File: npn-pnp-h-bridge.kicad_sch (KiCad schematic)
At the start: 41 parts, among them J1 S4B-PH-K-S_LF__SN_, J2 S2B-PH-K-S_LF__SN_, Q1 MMBT3904, Q2 MMBT3904, Q3 MMBT3904, Q4 MMBT3904

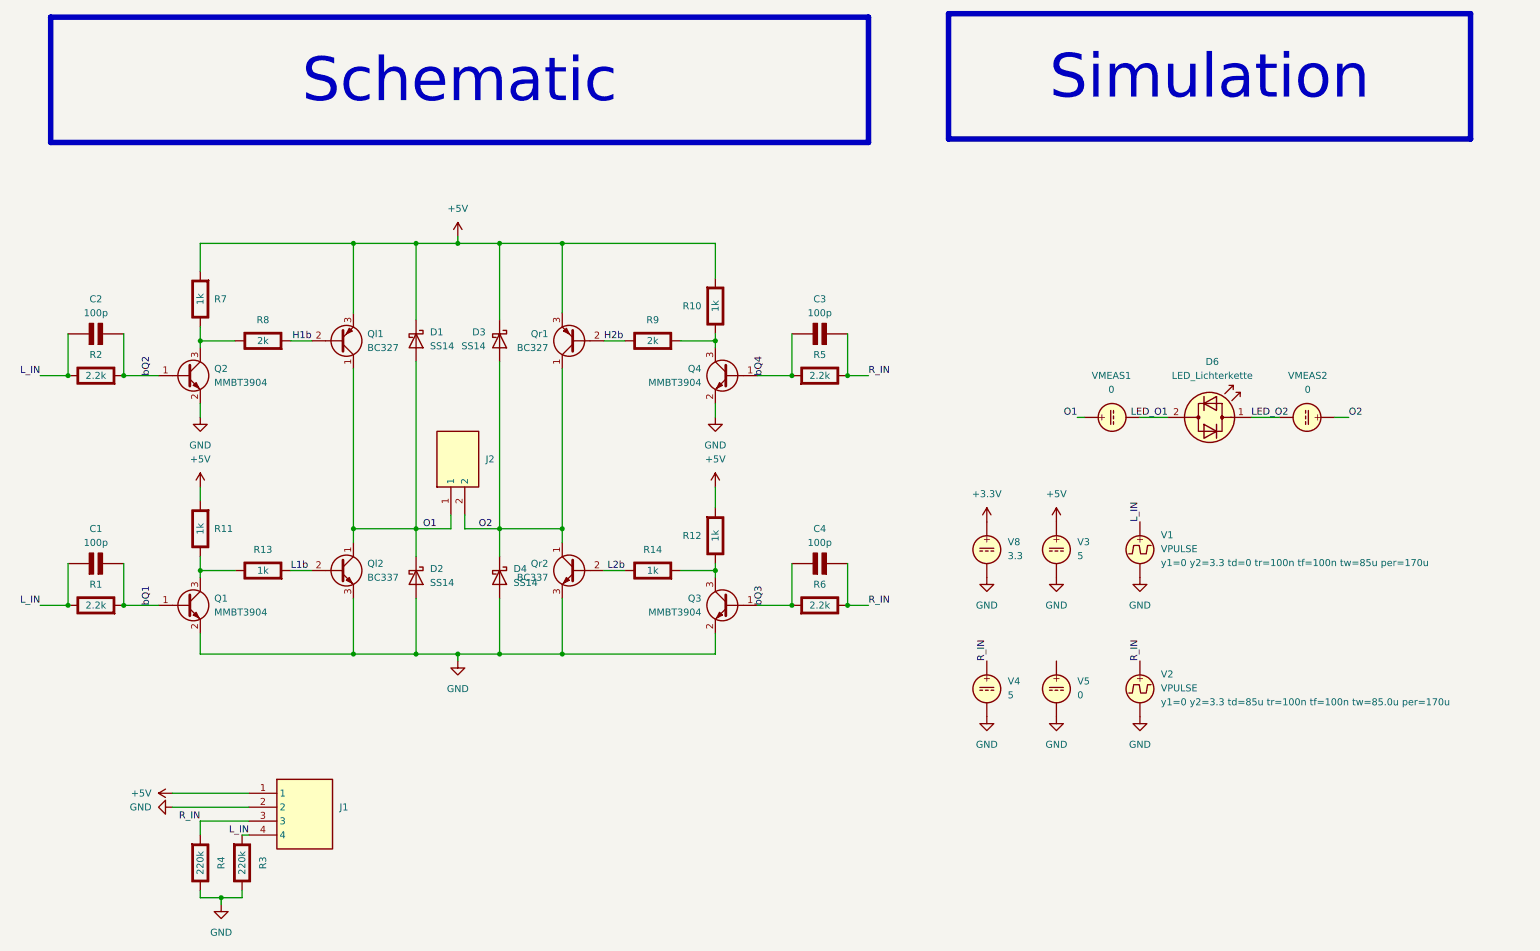
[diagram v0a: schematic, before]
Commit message: Update README with current measurements; optimize resistor values for up to 500mA load
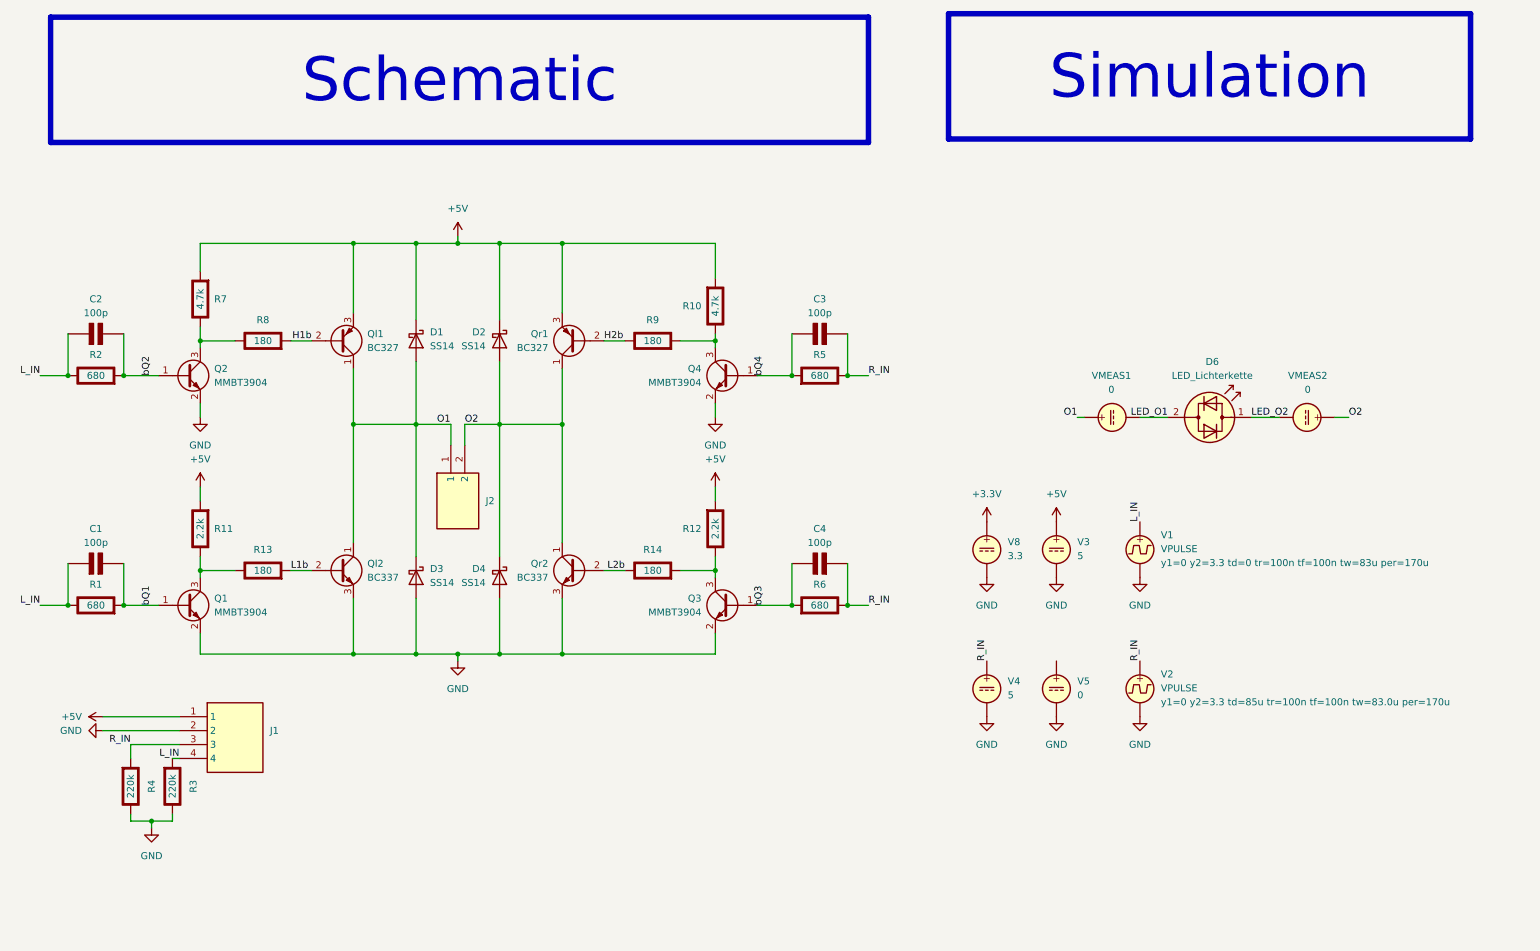
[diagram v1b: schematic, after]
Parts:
- R1, R2, R5, R6: value 2.2k -> 680
- R10, R7: value 1k -> 4.7k
- R11, R12: value 1k -> 2.2k
- R13, R14: value 1k -> 180
- R8, R9: value 2k -> 180
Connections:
- net +5V: now also D2.1 (K); no longer D3.1 (K)
- net GND: now also D3.2 (A); no longer D2.2 (A)
- net O1: now also D3.1 (K); no longer D2.1 (K)
- net O2: now also D2.2 (A); no longer D3.2 (A)
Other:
- moved on the sheet: J1, J2, R12, R3, R4

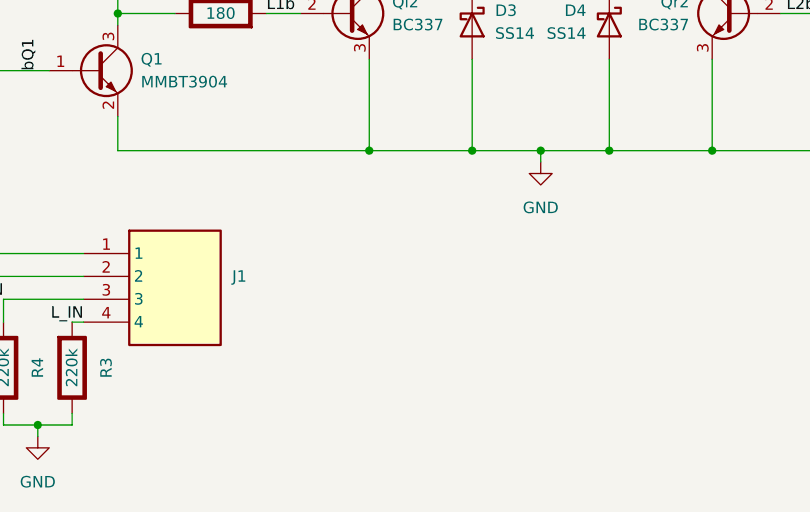
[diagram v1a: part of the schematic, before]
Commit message: Make PCB stackable via 2x03 connheader
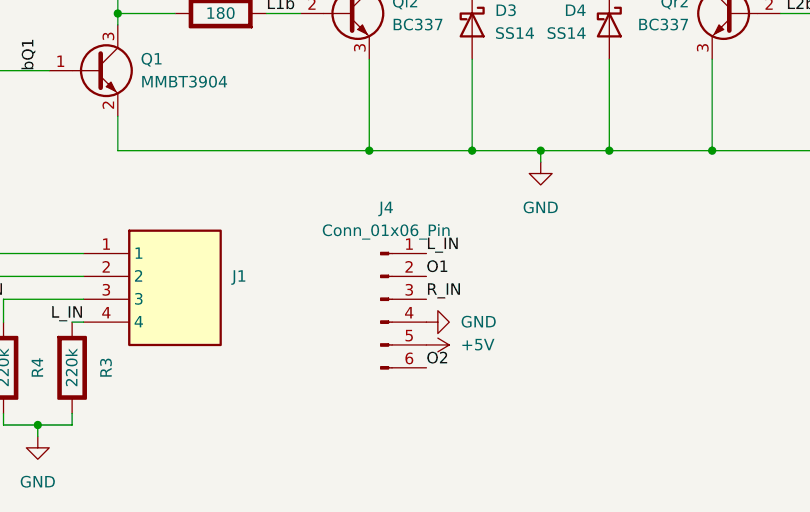
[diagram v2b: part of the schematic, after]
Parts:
- added J4: Conn_01x06_Pin, Connector_PinHeader_2.54mm:PinHeader_2x03_P2.54mm_Vertical, symbol Connector:Conn_01x06_Pin
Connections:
- net +5V: now also J4.5 (Pin_5)
- net GND: now also J4.4 (Pin_4)
- net L_IN: now also J4.1 (Pin_1)
- net O1: now also J4.2 (Pin_2)
- net O2: now also J4.6 (Pin_6)
- net R_IN: now also J4.3 (Pin_3)
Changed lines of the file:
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@@
 		)
 	)
+	(label "O1"
+		(at 81.28 154.94 0)
+		(effects
+			(font
+				(size 1.27 1.27)
+			)
+			(justify left bottom)
+		)
+	)
 	(label "H1b"
 		(at 67.31 83.82 180)
@@
 		)
 	)
+	(label "R_IN"
+		(at 81.28 157.48 0)
+		(effects
+			(font
+				(size 1.27 1.27)
+			)
+			(justify left bottom)
+		)
+	)
 	(label "O1"
 		(at 90.17 99.06 0)
@@
 	)
 	(label "L_IN"
+		(at 81.28 152.4 0)
+		(effects
+			(font
+				(size 1.27 1.27)
+			)
+			(justify left bottom)
+		)
+	)
+	(label "L_IN"
 		(at 218.44 116.84 90)
 		(effects
@@
 		)
 	)
+	(label "O2"
+		(at 81.28 165.1 0)
+		(effects
+			(font
+				(size 1.27 1.27)
+			)
+			(justify left bottom)
+		)
+	)
 	(label "bQ4"
 		(at 149.86 90.17 90)
@@
 	)
 	(symbol
+		(lib_id "Connector:Conn_01x06_Pin")
+		(at 76.2 157.48 0)
+		(unit 1)
+		(exclude_from_sim no)
+		(in_bom yes)
+		(on_board yes)
+		(dnp no)
+		(fields_autoplaced yes)
+		(property "Reference" "J4"
+			(at 76.835 147.32 0)
+			(effects
+				(font
+					(size 1.27 1.27)
+				)
+			)
+		)
+		(property "Value" "Conn_01x06_Pin"
+			(at 76.835 149.86 0)
+			(effects
+				(font
+					(size 1.27 1.27)
+				)
+			)
+		)
+		(property "Footprint" "Connector_PinHeader_2.54mm:PinHeader_2x03_P2.54mm_Vertical"
+			(at 76.2 157.48 0)
+			(effects
+				(font
+					(size 1.27 1.27)
+				)
+				(hide yes)
+			)
+		)
+		(property "Datasheet" "~"
+			(at 76.2 157.48 0)
+			(effects
+				(font
+					(size 1.27 1.27)
+				)
+				(hide yes)
+			)
+		)
+		(property "Description" "Generic connector, single row, 01x06, script generated"
+			(at 76.2 157.48 0)
+			(effects
+				(font
+					(size 1.27 1.27)
+				)
+				(hide yes)
+			)
+		)
+		(pin "5"
+		)
+		(pin "1"
+		)
+		(pin "6"
+		)
+		(pin "2"
+		)
+		(pin "3"
+		)
+		(pin "4"
+		)
+		(instances
+			(project "npn-pnp-h-bridge"
+				(path "/225c2104-9470-41e6-a40d-f9d3cc65f923"
+					(reference "J4")
+					(unit 1)
+				)
+			)
+		)
+	)
+	(symbol
 		(lib_id "Transistor_BJT:MMBT3904")
 		(at 44.45 90.17 0)
@@
 	(symbol
 		(lib_id "power:GND")
+		(at 81.28 160.02 90)
+		(unit 1)
+		(exclude_from_sim no)
+		(in_bom yes)
+		(on_board yes)
+		(dnp no)
+		(fields_autoplaced yes)
+		(property "Reference" "#PWR018"
+			(at 87.63 160.02 0)
+			(effects
+				(font
+					(size 1.27 1.27)
+				)
+				(hide yes)
+			)
+		)
+		(property "Value" "GND"
+			(at 85.09 160.0199 90)
+			(effects
+				(font
+					(size 1.27 1.27)
+				)
+				(justify right)
+			)
+		)
+		(property "Footprint" ""
+			(at 81.28 160.02 0)
+			(effects
+				(font
+					(size 1.27 1.27)
+				)
+				(hide yes)
+			)
+		)
+		(property "Datasheet" ""
+			(at 81.28 160.02 0)
+			(effects
+				(font
+					(size 1.27 1.27)
+				)
+				(hide yes)
+			)
+		)
+		(property "Description" "Power symbol creates a global label with name \"GND\" , ground"
+			(at 81.28 160.02 0)
+			(effects
+				(font
+					(size 1.27 1.27)
+				)
+				(hide yes)
+			)
+		)
+		(pin "1"
+		)
+		(instances
+			(project "npn-pnp-h-bridge"
+				(path "/225c2104-9470-41e6-a40d-f9d3cc65f923"
+					(reference "#PWR018")
+					(unit 1)
+				)
+			)
+		)
+	)
+	(symbol
+		(lib_id "power:GND")
 		(at 203.2 127 0)
 		(unit 1)
@@
 					(unit 1)
 				)
+			)
+		)
+	)
+	(symbol
+		(lib_id "power:+5V")
+		(at 81.28 162.56 270)
+		(unit 1)
+		(exclude_from_sim no)
+		(in_bom yes)
+		(on_board yes)
+		(dnp no)
+		(fields_autoplaced yes)
+		(property "Reference" "#PWR014"
+			(at 77.47 162.56 0)
+			(effects
+				(font
+					(size 1.27 1.27)
+				)
+				(hide yes)
+			)
+		)
+		(property "Value" "+5V"
+			(at 85.09 162.5599 90)
+			(effects
+				(font
+					(size 1.27 1.27)
+				)
+				(justify left)
+			)
+		)
+		(property "Footprint" ""
+			(at 81.28 162.56 0)
+			(effects
+				(font
+					(size 1.27 1.27)
+				)
+				(hide yes)
+			)
+		)
+		(property "Datasheet" ""
+			(at 81.28 162.56 0)
+			(effects
+				(font
+					(size 1.27 1.27)
+				)
+				(hide yes)
+			)
+		)
+		(property "Description" "Power symbol creates a global label with name \"+5V\""
+			(at 81.28 162.56 0)
+			(effects
+				(font
+					(size 1.27 1.27)
+				)
+				(hide yes)
+			)
+		)
+		(pin "1"
+		)
+		(instances
+			(project "npn-pnp-h-bridge"
+				(path "/225c2104-9470-41e6-a40d-f9d3cc65f923"
+					(reference "#PWR014")
+					(unit 1)
+				)

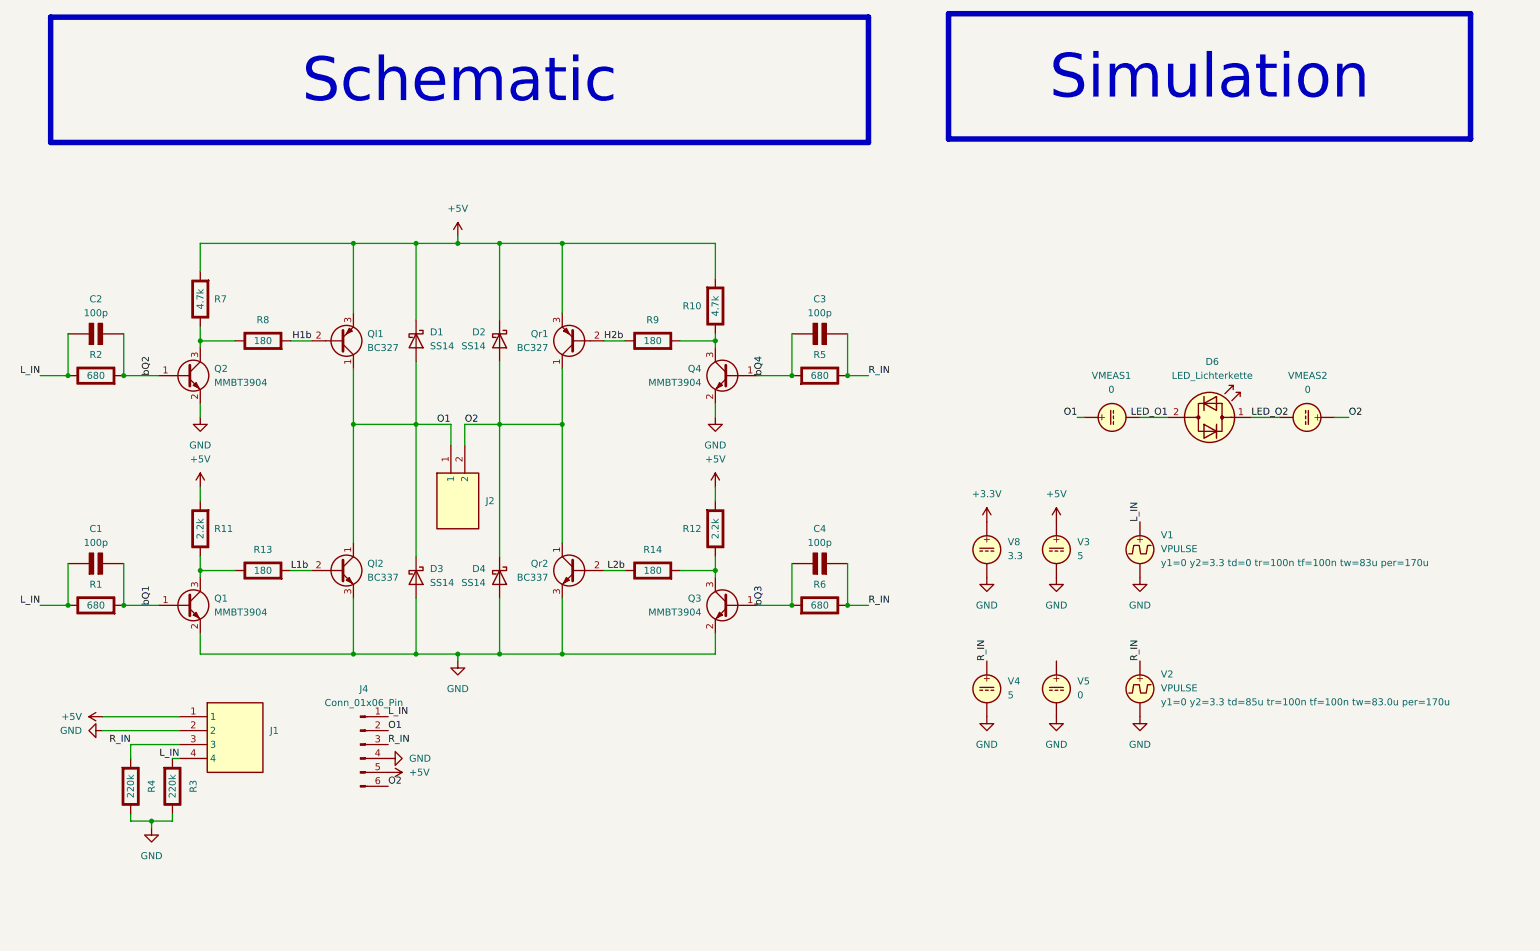
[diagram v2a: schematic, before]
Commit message: add caps to gnd for the h-bridge bases
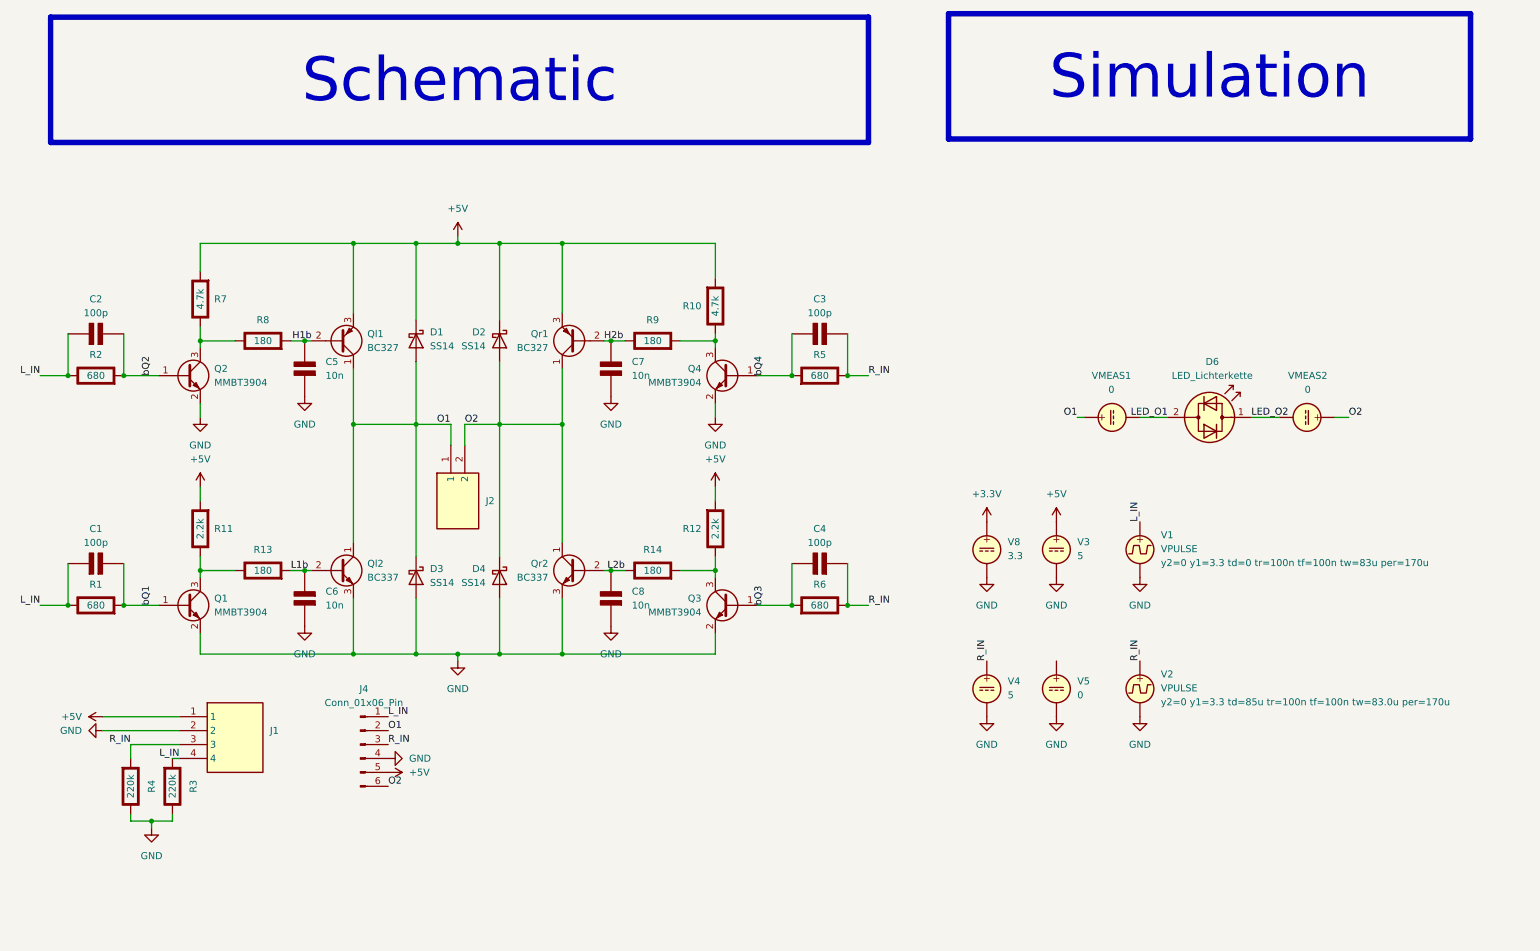
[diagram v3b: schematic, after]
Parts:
- added C5, C6, C7, C8: 10n, Capacitor_SMD:C_0805_2012Metric_Pad1.18x1.45mm_HandSolder, symbol PCM_Elektuur:C
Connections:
- net GND: now also C5.1 (+), C6.1 (+), C7.1 (+), C8.1 (+)
- net H1b: now also C5.2 (-)
- net H2b: now also C7.2 (-)
- net L1b: now also C6.2 (-)
- net L2b: now also C8.2 (-)
